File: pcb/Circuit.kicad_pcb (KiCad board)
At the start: 2 copper layers, 82.4 x 68.9 mm, 47 parts, among them J1 DTM13-12PA-R008, J2 TSW-101-07-T-D, J3 TSW-101-07-T-D, U1 MCP1700-1802E_TO92, U2 CDP68HC68S1, U3 LM2672N-5.0, U4 Teensy4.0, U5 MCP2562-H-P

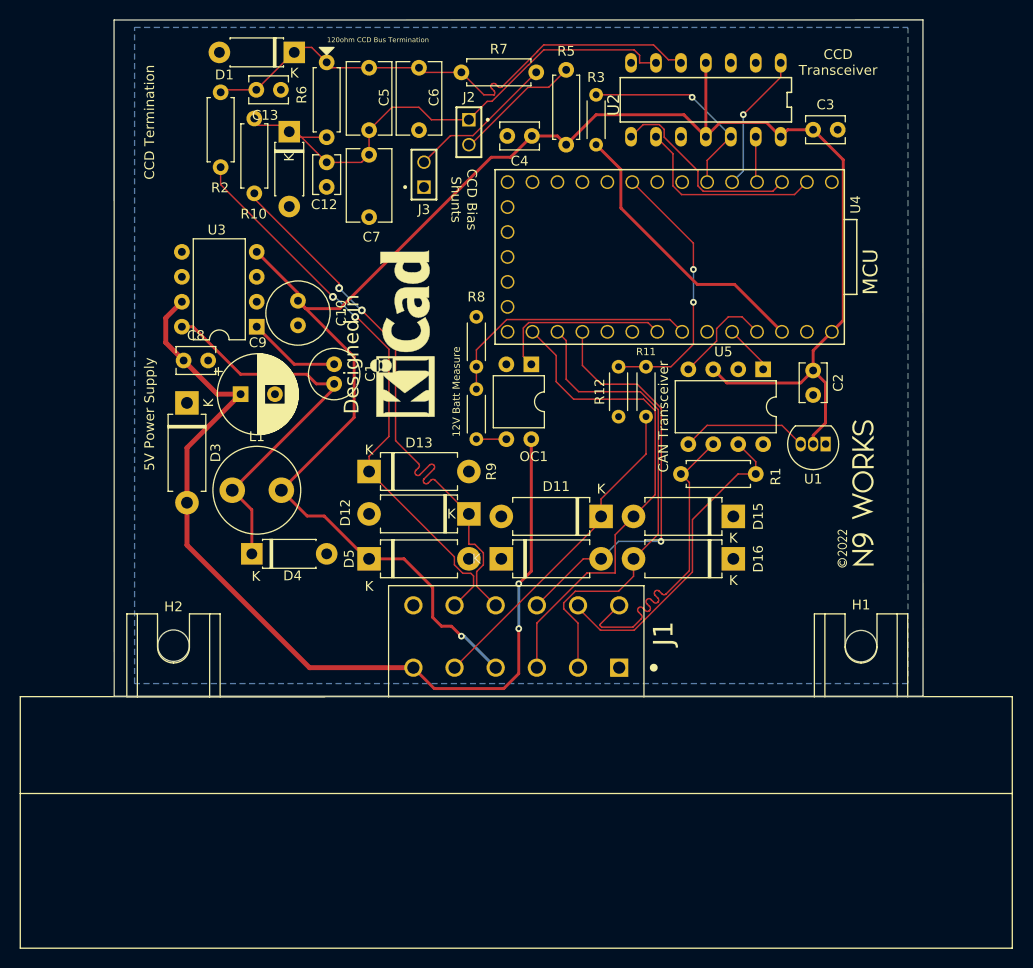
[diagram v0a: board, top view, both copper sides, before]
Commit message: Tidy up capacitors
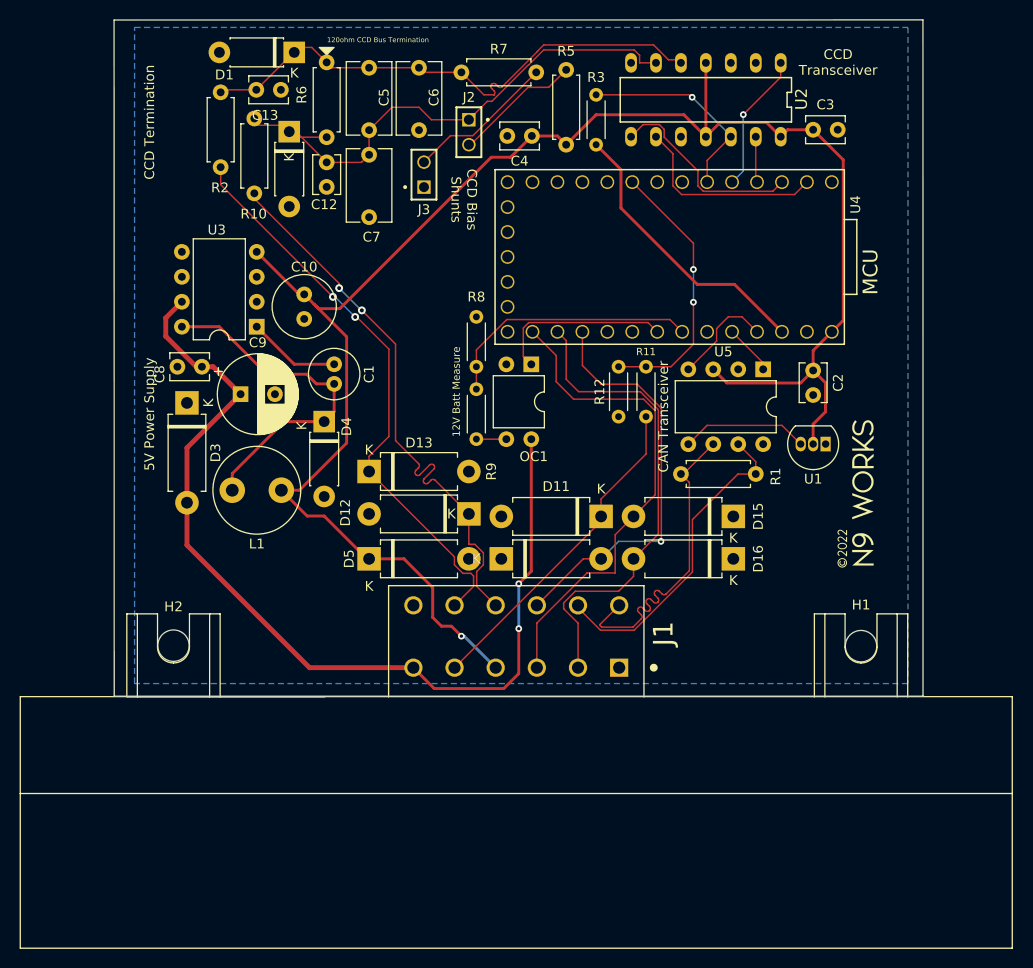
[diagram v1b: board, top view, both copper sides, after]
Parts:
- moved D4 15.3 mm to (71.6, 107.4), turned to -90 degrees
- moved C8 1.97 mm to (59.2, 101.9), turned to 180 degrees
- moved C10 0.91 mm to (69.6, 94.5)
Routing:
- net Net-(C1-Pad2): track 40.3 -> 35.4 mm
- net +5V: track 181.0 -> 180.0 mm
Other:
- board text added: "Shunt the CCD bias resistors (J2/J3) if no other node provides them."
- board text removed: "Shunt the CCD bias resistors if no other node provides them."

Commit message: move via cleanup
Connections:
- U4 pad 21: IO/2 -> IO/3
- U4 pad 22: IO/1 -> IO/2
- U4 pad 23: IO/3 -> IO/1
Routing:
- net IO/2: track 50.2 -> 43.9 mm, vias 0 -> 2
- net IO/3: track 42.2 -> 36.0 mm, vias 1 -> 2
- net +12V: track 96.7 -> 91.1 mm
- net IO/1: track 49.3 -> 44.2 mm, vias 0 -> 2
- net can-: track 33.4 -> 32.0 mm
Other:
- board text added: "Extended I/Os IO/1 = Teensy A2(P16) IO/2 = Teensy A1(P15), RX3 w/PWM IO/3 = Teensy A0(P14), TX3 w/PWM"
- board text removed: "Extended I/Os IO/1 = Teensy A1(P15), RX3 w/PWM IO/2 = Teensy A0(P14), TX3 w/PWM IO/3 = Teensy A2(P16)"
